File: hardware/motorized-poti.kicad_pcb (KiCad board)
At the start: 2 copper layers, 100 x 20 mm, 29 parts, among them J1 AKL_5_2, P1 CON-SENSOR2, P2 MOTORIZED_POTI, P3 BOOT, P4 CONN_02X04, P5 CONN_02X04, U1 XMC1XXX24, U2 ZXBM5210, U3 DRILL, U4 DRILL, U5 DRILL, U6 DRILL

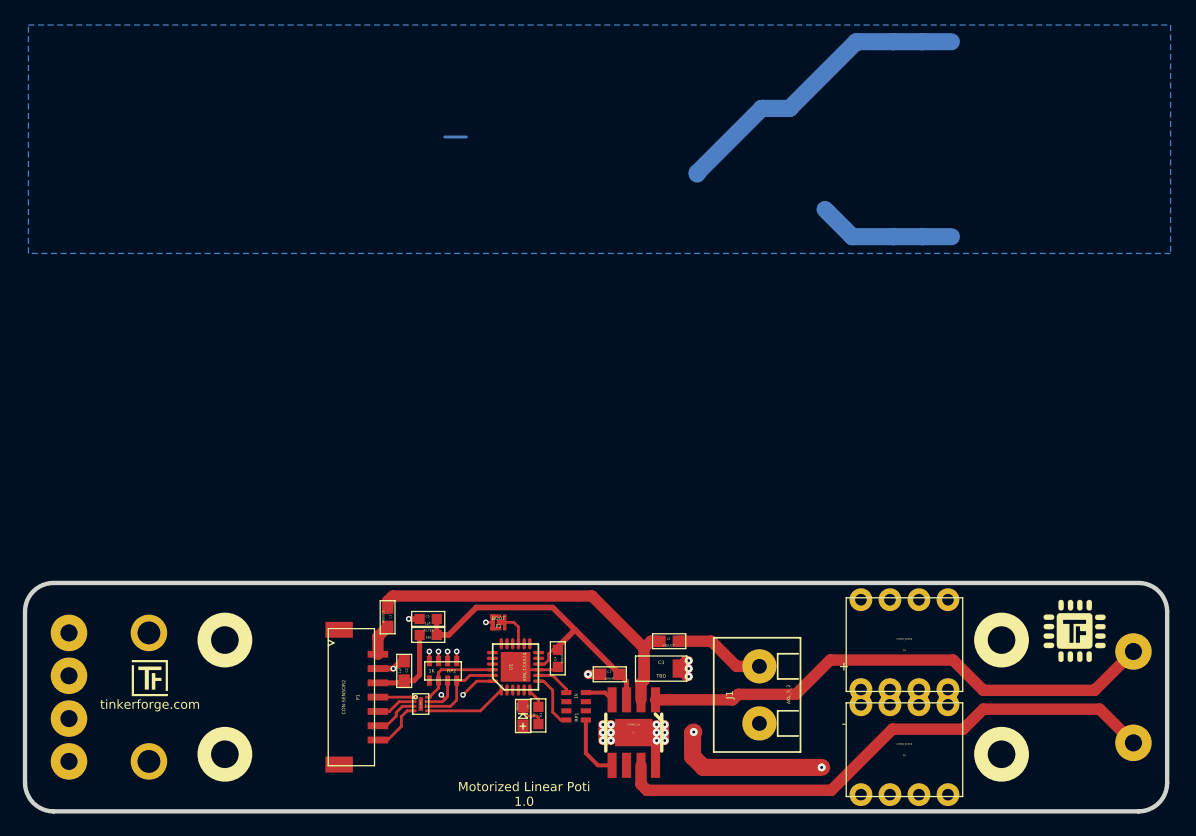
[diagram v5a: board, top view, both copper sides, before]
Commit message: Change filtering to R/C circuit
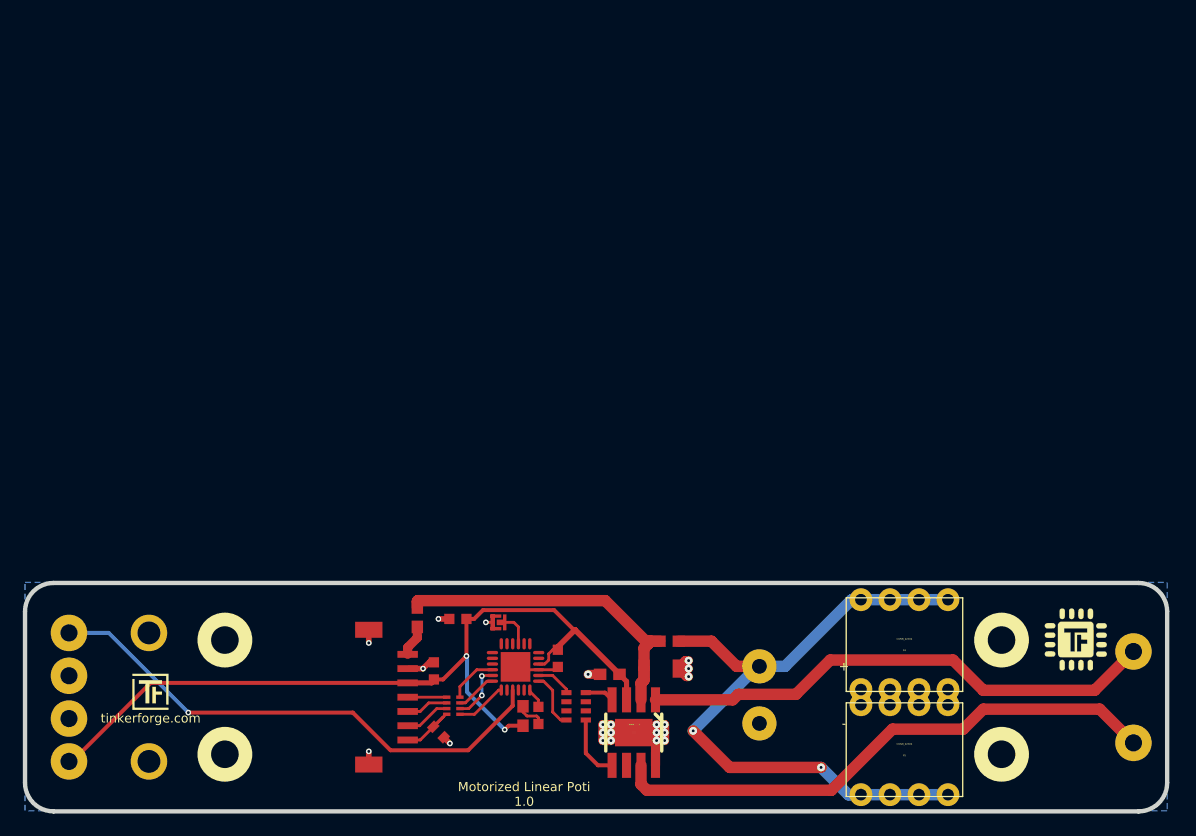
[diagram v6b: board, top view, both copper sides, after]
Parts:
- removed FB1: FILTER, 0603F
- removed FILTER1: Filter-4x, kicad-libraries:DFN8-17x135
- removed RP2: 1K, kicad-libraries:0603X4
- added C6: TBD, C0402E, F.Cu at (113.8, 103.7)
- added RP3: TBD, 4X0402, F.Cu at (115.1, 101.4)
- C1: footprint kicad-libraries:0603E -> kicad-libraries:C0603E
- C2: footprint kicad-libraries:0603E -> C0603F
- C3: footprint kicad-libraries:1206 -> kicad-libraries:C1206
- C4, C5: footprint 0603F -> C0603F
- J1: footprint kicad-libraries:AKL_5_2 -> AKL_5_2
- L1, L2: footprint kicad-libraries:0603E -> C0603E
- P2: footprint kicad-libraries:MOTORIZED_POTI -> MOTORIZED_POTI
- R1: footprint 0603F -> R0603F
- RP1: footprint kicad-libraries:4X0603 -> 4X0603
- U2: footprint kicad-libraries:SO-8-EP -> SO-8-EP
- moved G*** 15.4 mm to (116.4, 100.6)
- moved VAL 14.1 mm to (106.4, 100.6), turned to 0 degrees
- moved C2 2.60 mm to (113.4, 98.3)
- moved L1 2.60 mm to (112.0, 93.7)
- moved C5 2.60 mm to (115.5, 93.8)
- moved P1 2.60 mm to (106.5, 100.7)
- moved G*** 1.20 mm to (87.0, 98.6)
- moved G*** 0.76 mm to (169.6, 95.6)
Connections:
- C2 pad 1: Net-(C2-Pad1) -> VCC
- P1 pad 3: Net-(C2-Pad1) -> VCC
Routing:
- net (no net): track 55.0 -> 0.00 mm, vias 2 -> 0
- net PWR: track 7.96 -> 59.7 mm, vias 0 -> 2
- net VCC: track 28.2 -> 74.9 mm, vias 0 -> 2
- net AIN: track 0.00 -> 46.1 mm, vias 0 -> 1
- net Net-(C2-Pad1): track 7.44 -> 0.00 mm
- net S-CLK: track 6.83 -> 3.64 mm, vias 2 -> 0
- net S-CS: track 7.38 -> 4.39 mm
- net S-MOSI: track 7.71 -> 5.05 mm, vias 0 -> 2
- net S-MISO: track 7.13 -> 4.50 mm
- net Net-(C3-Pad2): track 31.3 -> 29.3 mm
- net Net-(C6-Pad1): track 4.63 -> 6.41 mm
- net Net-(P1-Pad6): track 3.95 -> 4.80 mm
- net GND: track 35.0 -> 34.7 mm, vias 23 -> 22

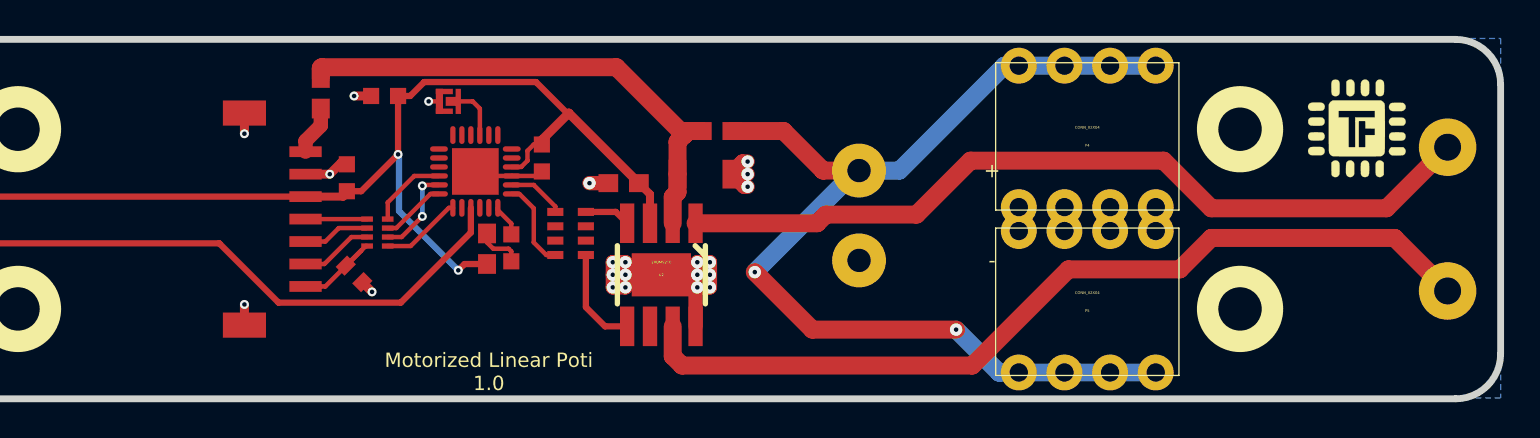
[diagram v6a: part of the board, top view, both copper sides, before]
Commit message: Move LED pin; add fiducial marks
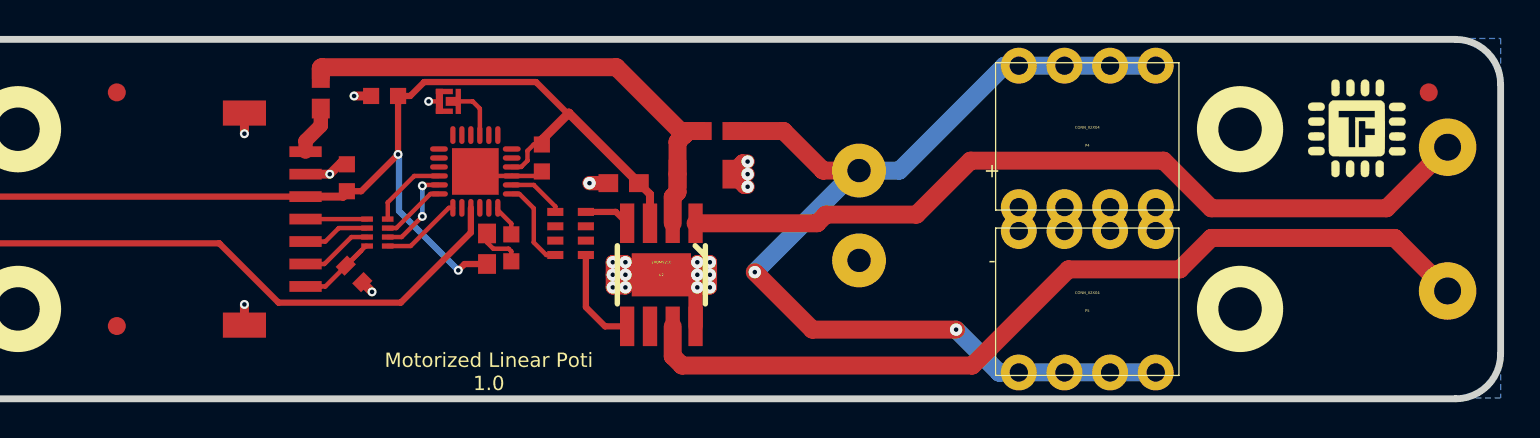
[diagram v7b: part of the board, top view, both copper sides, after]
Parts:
- added Fiducial_Mark: VAL**, kicad-libraries:Fiducial_Mark, F.Cu at (100.6, 93.6)
- added Fiducial_Mark: VAL**, kicad-libraries:Fiducial_Mark, F.Cu at (100.6, 106.6)
- added Fiducial_Mark: VAL**, kicad-libraries:Fiducial_Mark, F.Cu at (173.6, 93.6)
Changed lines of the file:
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@@
     (links 70)
     (no_connects 5)
-    (area 70.875139 90.459499 282.895869 162.490743)
+    (area 77.409499 90.459499 177.790501 110.840501)
     (thickness 1.6002)
     (drawings 13)
     (tracks 211)
     (zones 0)
-    (modules 28)
+    (modules 31)
     (nets 42)
   )
@@
     (34 B.Paste user)
     (35 F.Paste user)
-    (36 B.SilkS user hide)
+    (36 B.SilkS user)
     (37 F.SilkS user)
     (38 B.Mask user)
@@
       (net 1 GND))
   )
+  (module kicad-libraries:Fiducial_Mark (layer Vorderseite)
+    (at 100.6 93.6)
+    (attr smd)
+    (fp_text reference Fiducial_Mark (at 0 0) (layer F.SilkS) hide
+      (effects (font (size 0.127 0.127) (thickness 0.03302)))
+    )
+    (fp_text value VAL** (at 0 -0.29972) (layer F.SilkS) hide
+      (effects (font (size 0.127 0.127) (thickness 0.03302)))
+    )
+    (fp_circle (center 0 0) (end 1.15062 0) (layer Dwgs.User) (width 0.01016))
+    (pad 1 smd circle (at 0 0) (size 1.00076 1.00076) (layers Vorderseite F.Paste F.Mask)
+      (clearance 0.65024))
+  )
+  (module kicad-libraries:Fiducial_Mark (layer Vorderseite)
+    (at 100.6 106.6)
+    (attr smd)
+    (fp_text reference Fiducial_Mark (at 0 0) (layer F.SilkS) hide
+      (effects (font (size 0.127 0.127) (thickness 0.03302)))
+    )
+    (fp_text value VAL** (at 0 -0.29972) (layer F.SilkS) hide
+      (effects (font (size 0.127 0.127) (thickness 0.03302)))
+    )
+    (fp_circle (center 0 0) (end 1.15062 0) (layer Dwgs.User) (width 0.01016))
+    (pad 1 smd circle (at 0 0) (size 1.00076 1.00076) (layers Vorderseite F.Paste F.Mask)
+      (clearance 0.65024))
+  )
+  (module kicad-libraries:Fiducial_Mark (layer Vorderseite)
+    (at 173.6 93.6)
+    (attr smd)
+    (fp_text reference Fiducial_Mark (at 0 0) (layer F.SilkS) hide
+      (effects (font (size 0.127 0.127) (thickness 0.03302)))
+    )
+    (fp_text value VAL** (at 0 -0.29972) (layer F.SilkS) hide
+      (effects (font (size 0.127 0.127) (thickness 0.03302)))
+    )
+    (fp_circle (center 0 0) (end 1.15062 0) (layer Dwgs.User) (width 0.01016))
+    (pad 1 smd circle (at 0 0) (size 1.00076 1.00076) (layers Vorderseite F.Paste F.Mask)
+      (clearance 0.65024))
+  )
   (gr_line (start 77.6 93.15) (end 77.6 108.15) (angle 90) (layer Edge.Cuts) (width 0.381))

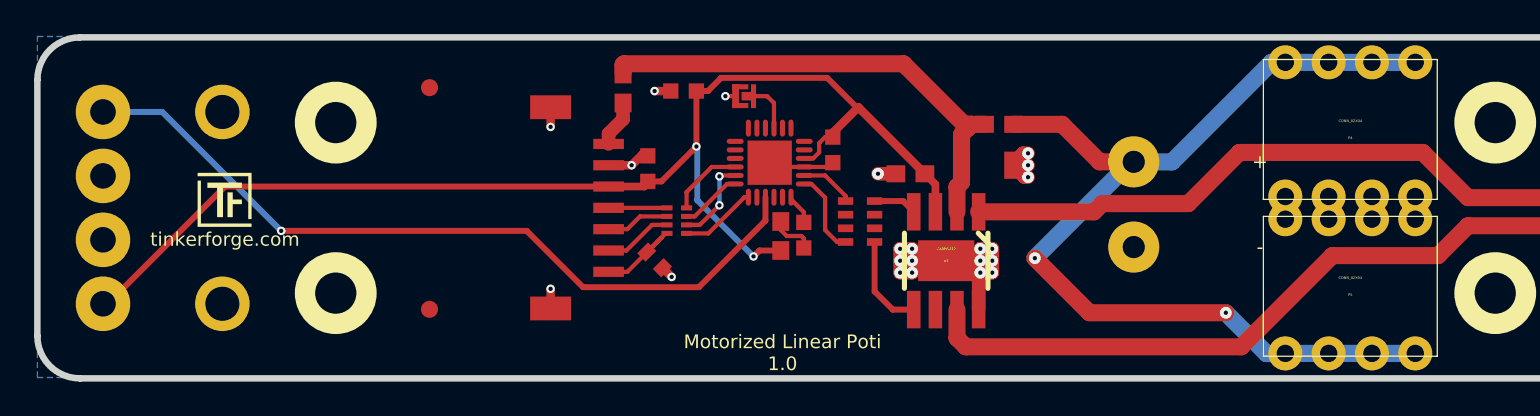
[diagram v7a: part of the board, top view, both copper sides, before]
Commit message: some footprints fixed, fix routing
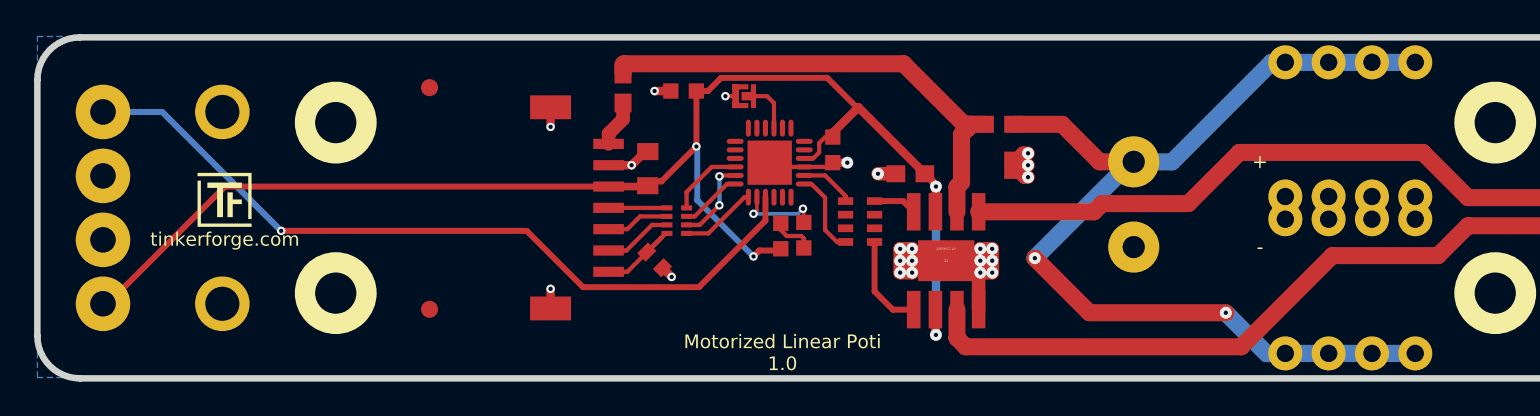
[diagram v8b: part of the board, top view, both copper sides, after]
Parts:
- C2: value 1µF -> 10µF; footprint C0603F -> kicad-libraries:C0805
- C4, C5: footprint C0603F -> kicad-libraries:C0603F
- C6: footprint C0402E -> kicad-libraries:C0402E
- D1: footprint D0603E -> kicad-libraries:D0603F
- J1: footprint AKL_5_2 -> kicad-libraries:AKL_5_2
- L1, L2: footprint C0603E -> kicad-libraries:C0603E
- P1: footprint CON-SENSOR2 -> kicad-libraries:CON-SENSOR2
- P2: footprint MOTORIZED_POTI -> kicad-libraries:MOTORIZED_POTI
- R1: footprint R0603F -> kicad-libraries:R0603F
- RP1: footprint 4X0603 -> kicad-libraries:4X0603
- RP3: footprint 4X0402 -> kicad-libraries:4X0402
- U2: footprint SO-8-EP -> kicad-libraries:SO-8-EP
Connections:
- P2 pad 2: Net-(P2-Pad2) -> (no net)
- RP1 pad 2: Net-(RP1-Pad2) -> (no net)
- RP1 pad 3: Net-(RP1-Pad3) -> (no net)
- RP1 pad 6: Net-(RP1-Pad6) -> (no net)
- RP1 pad 7: Net-(RP1-Pad7) -> (no net)
- U1 pad 11: Net-(U1-Pad11) -> (no net)
- U1 pad 12: Net-(U1-Pad12) -> (no net)
- U1 pad 13: Net-(U1-Pad13) -> (no net)
- U1 pad 14: Net-(U1-Pad14) -> (no net)
- U1 pad 16: Net-(U1-Pad16) -> (no net)
- U1 pad 17: Net-(U1-Pad17) -> (no net)
- U1 pad 18: Net-(U1-Pad18) -> (no net)
- U1 pad 19: Net-(U1-Pad19) -> (no net)
- U1 pad 2: Net-(U1-Pad2) -> Net-(R1-Pad2)
- U1 pad 20: Net-(U1-Pad20) -> (no net)
- U1 pad 21: Net-(U1-Pad21) -> (no net)
- U1 pad 4: Net-(U1-Pad4) -> (no net)
- U1 pad 5: Net-(U1-Pad5) -> (no net)
- U1 pad 6: Net-(R1-Pad2) -> (no net)
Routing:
- net VCC: track 74.9 -> 85.1 mm, vias 2 -> 4
- net GND: track 34.7 -> 38.1 mm, vias 22 -> 23
- net Net-(R1-Pad2): track 1.79 -> 4.90 mm, vias 0 -> 2
- net Net-(P2-Pad2): track 0.53 -> 0.00 mm
